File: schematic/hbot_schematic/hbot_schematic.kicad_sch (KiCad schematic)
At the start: 23 parts, among them M1 Nema 17, M2 Nema 23, M3 Nema 17, M4 Nema 14, M5 Nema 14, M6 Nema 14, U1 Teensy4.1

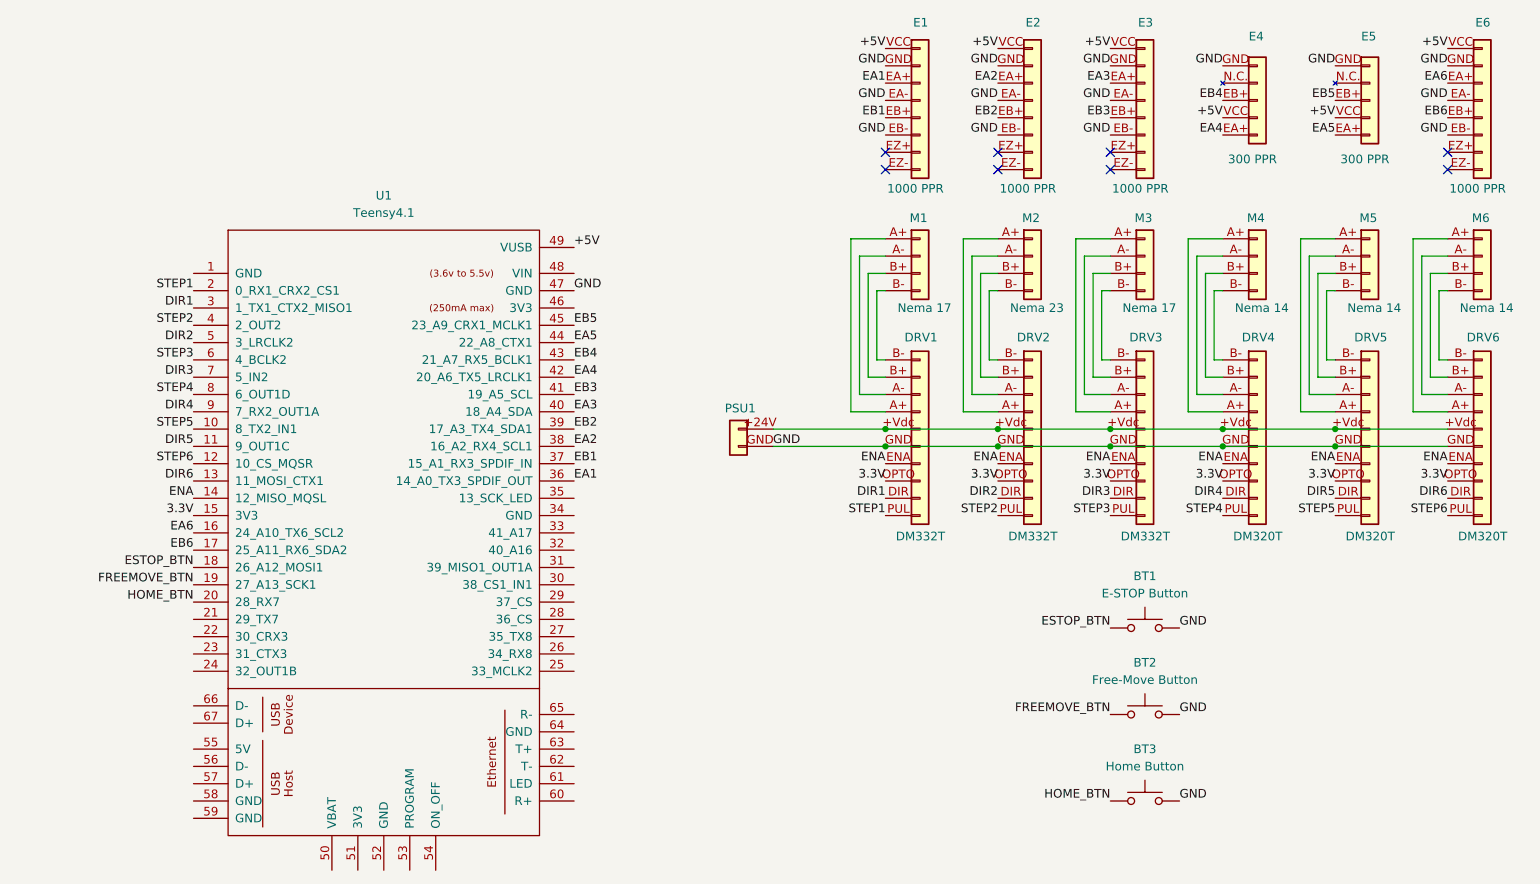
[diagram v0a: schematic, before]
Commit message: updated with hardware E-stop + software for redundancy. ujdpated readme, added schematic
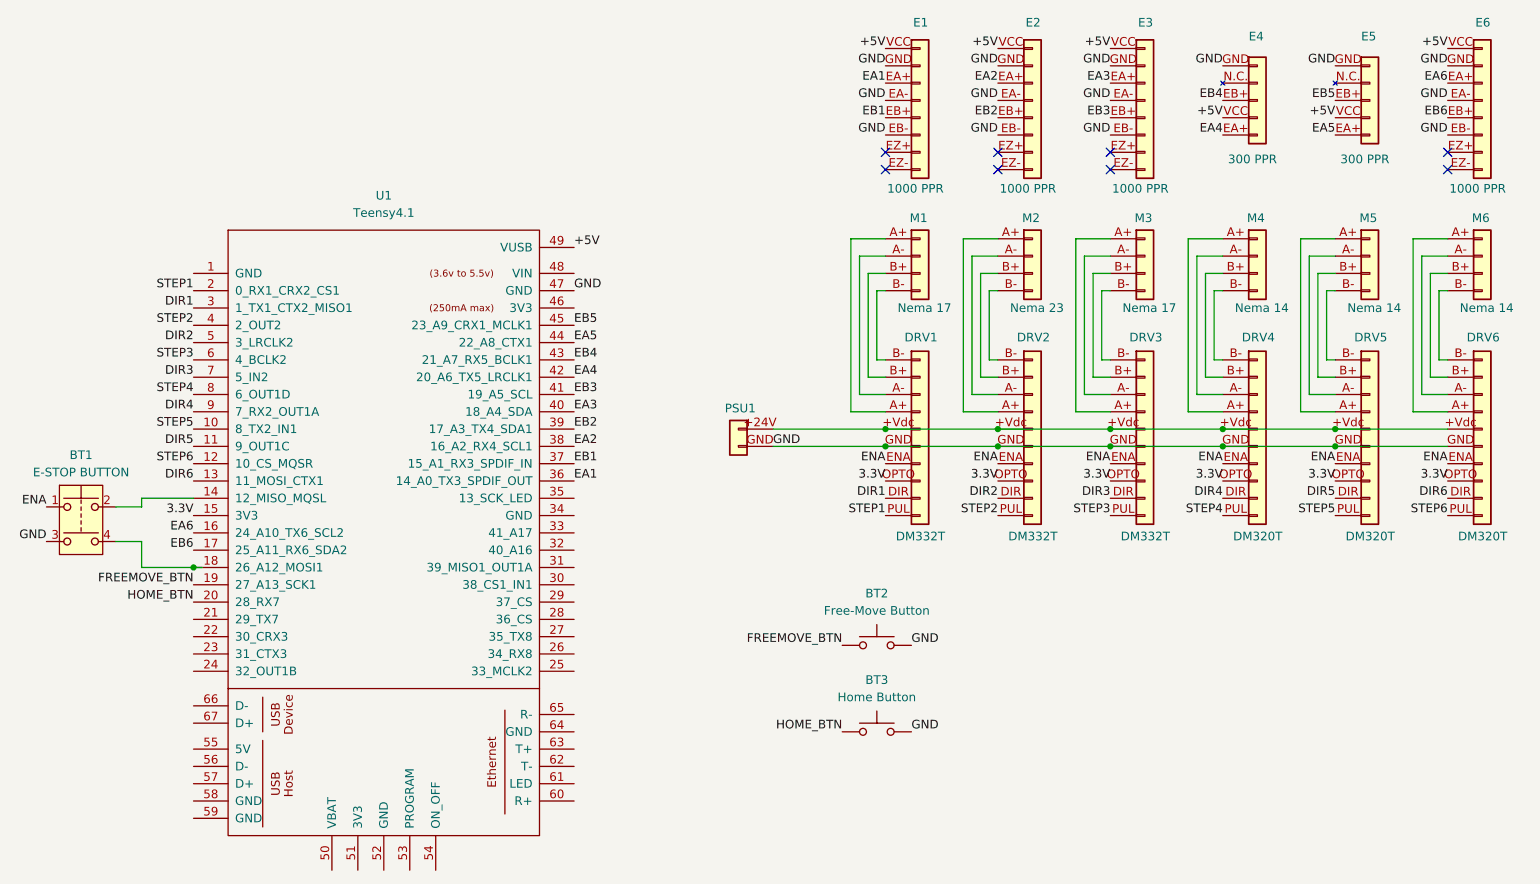
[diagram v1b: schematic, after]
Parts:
- removed BT1: E-STOP Button, symbol Switch:SW_Push
- added BT1: E-STOP BUTTON, symbol Switch:SW_Push_Dual
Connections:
- net ENA: now also BT1.1; no longer U1.14 (12_MISO_MQSL)
- net GND: now also BT1.3
- net ESTOP_BTN: no longer names the net of U1.18 (26_A12_MOSI1)
- net ESTOP_BTN: now also BT1.4
- new net: BT1.2, U1.14 (12_MISO_MQSL)
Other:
- moved on the sheet: BT2, BT3
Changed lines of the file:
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@@
 	)
 	(junction
+		(at 62.23 111.76)
+		(diameter 0)
+		(color 0 0 0 0)
+	)
+	(junction
 		(at 196.85 93.98)
 		(diameter 0)
@@
 	(wire
 		(pts
+			(xy 62.23 101.6) (xy 54.61 101.6)
+		)
+		(stroke
+			(width 0)
+			(type default)
+		)
+	)
+	(wire
+		(pts
 			(xy 193.04 66.04) (xy 196.85 66.04)
 		)
@@
 	(wire
 		(pts
+			(xy 54.61 107.95) (xy 54.61 111.76)
+		)
+		(stroke
+			(width 0)
+			(type default)
+		)
+	)
+	(wire
+		(pts
 			(xy 180.34 91.44) (xy 196.85 91.44)
 		)
@@
 	(wire
 		(pts
+			(xy 50.8 107.95) (xy 54.61 107.95)
+		)
+		(stroke
+			(width 0)
+			(type default)
+		)
+	)
+	(wire
+		(pts
 			(xy 196.85 81.28) (xy 195.58 81.28)
 		)
@@
 	(wire
 		(pts
+			(xy 54.61 111.76) (xy 62.23 111.76)
+		)
+		(stroke
+			(width 0)
+			(type default)
+		)
+	)
+	(wire
+		(pts
 			(xy 195.58 81.28) (xy 195.58 71.12)
 		)
@@
 	(wire
 		(pts
+			(xy 54.61 101.6) (xy 54.61 102.87)
+		)
+		(stroke
+			(width 0)
+			(type default)
+		)
+	)
+	(wire
+		(pts
 			(xy 213.36 81.28) (xy 212.09 81.28)
 		)
@@
 	(wire
 		(pts
+			(xy 62.23 111.76) (xy 63.5 111.76)
+		)
+		(stroke
+			(width 0)
+			(type default)
+		)
+	)
+	(wire
+		(pts
 			(xy 180.34 86.36) (xy 176.53 86.36)
 		)
@@
 		)
 	)
+	(wire
+		(pts
+			(xy 54.61 102.87) (xy 50.8 102.87)
+		)
+		(stroke
+			(width 0)
+			(type default)
+		)
+	)
 	(label "STEP4"
 		(at 62.23 86.36 180)
@@
 		)
 	)
-	(label "ENA"
-		(at 62.23 101.6 180)
-		(effects
-			(font
-				(size 1.27 1.27)
-			)
-			(justify right bottom)
-		)
-	)
 	(label "GND"
 		(at 246.38 43.18 180)
@@
 		)
 	)
-	(label "ESTOP_BTN"
-		(at 196.85 120.65 180)
-		(effects
-			(font
-				(size 1.27 1.27)
-			)
-			(justify right bottom)
-		)
-	)
 	(label "HOME_BTN"
-		(at 196.85 146.05 180)
+		(at 157.48 135.89 180)
 		(effects
 			(font
@@
 	)
 	(label "FREEMOVE_BTN"
-		(at 196.85 133.35 180)
+		(at 157.48 123.19 180)
 		(effects
 			(font
@@
 	)
 	(label "GND"
-		(at 207.01 120.65 0)
+		(at 167.64 123.19 0)
 		(effects
 			(font
@@
 	)
 	(label "GND"
-		(at 207.01 133.35 0)
+		(at 167.64 135.89 0)
 		(effects
 			(font
@@
 		)
 	)
-	(label "GND"
-		(at 207.01 146.05 0)
+	(label "ENA"
+		(at 40.64 102.87 180)
 		(effects
 			(font
 				(size 1.27 1.27)
 			)
-			(justify left bottom)
+			(justify right bottom)
 		)
 	)
@@
 		)
 	)
-	(label "FREEMOVE_BTN"
-		(at 62.23 114.3 180)
+	(label "GND"
+		(at 40.64 107.95 180)
 		(effects
 			(font
@@
 		)
 	)
-	(label "DIR1"
-		(at 62.23 73.66 180)
+	(label "FREEMOVE_BTN"
+		(at 62.23 114.3 180)
 		(effects
 			(font
@@
 		)
 	)
-	(label "ESTOP_BTN"
-		(at 62.23 111.76 180)
+	(label "DIR1"
+		(at 62.23 73.66 180)
 		(effects
 			(font
@@
 	)
 	(symbol
-		(lib_id "Switch:SW_Push")
-		(at 201.93 120.65 0)
-		(unit 1)
-		(exclude_from_sim no)
-		(in_bom yes)
-		(on_board yes)
-		(dnp no)
-		(fields_autoplaced yes)
-		(property "Reference" "BT1"
-			(at 201.93 113.03 0)
-			(effects
-				(font
-					(size 1.27 1.27)
-				)
-			)
-		)
-		(property "Value" "E-STOP Button"
-			(at 201.93 115.57 0)
-			(effects
-				(font
-					(size 1.27 1.27)
-				)
-			)
-		)
-		(property "Footprint" ""
-			(at 201.93 115.57 0)
-			(effects
-				(font
-					(size 1.27 1.27)
-				)
-				(hide yes)
-			)
-		)
-		(property "Datasheet" "~"
-			(at 201.93 115.57 0)
-			(effects
-				(font
-					(size 1.27 1.27)
-				)
-				(hide yes)
-			)
-		)
-		(property "Description" "Push button switch, generic, two pins"
-			(at 201.93 120.65 0)
-			(effects
-				(font
-					(size 1.27 1.27)
-				)
-				(hide yes)
-			)
-		)
-		(pin "2"
-		)
-		(pin "1"
-		)
-		(instances
-			(project ""
-				(path "/bc1e725a-6633-4704-8d72-fa9ba85f98b3"
-					(reference "BT1")
-					(unit 1)
-				)
-			)
-		)
-	)
-	(symbol
 		(lib_id "Connector_Generic:Conn_01x04")
 		(at 168.91 66.04 0)
@@
 	(symbol
 		(lib_id "Switch:SW_Push")
-		(at 201.93 133.35 0)
+		(at 162.56 123.19 0)
 		(unit 1)
 		(exclude_from_sim no)
@@
 		(fields_autoplaced yes)
 		(property "Reference" "BT2"
-			(at 201.93 125.73 0)
+			(at 162.56 115.57 0)
 			(effects
 				(font
@@
 		)
 		(property "Value" "Free-Move Button"
-			(at 201.93 128.27 0)
+			(at 162.56 118.11 0)
 			(effects
 				(font
@@
 		)
 		(property "Footprint" ""
-			(at 201.93 128.27 0)
+			(at 162.56 118.11 0)
 			(effects
 				(font
@@
 		)
 		(property "Datasheet" "~"
-			(at 201.93 128.27 0)
+			(at 162.56 118.11 0)
 			(effects
 				(font
@@
 		)
 		(property "Description" "Push button switch, generic, two pins"
-			(at 201.93 133.35 0)
+			(at 162.56 123.19 0)
 			(effects
 				(font
@@
 	(symbol
 		(lib_id "Switch:SW_Push")
-		(at 201.93 146.05 0)
+		(at 162.56 135.89 0)
 		(unit 1)
 		(exclude_from_sim no)
@@
 		(fields_autoplaced yes)
 		(property "Reference" "BT3"
-			(at 201.93 138.43 0)
+			(at 162.56 128.27 0)
 			(effects
 				(font
@@
 		)
 		(property "Value" "Home Button"
-			(at 201.93 140.97 0)
+			(at 162.56 130.81 0)
 			(effects
 				(font
@@
 		)
 		(property "Footprint" ""
-			(at 201.93 140.97 0)
+			(at 162.56 130.81 0)
 			(effects
 				(font
@@
 		)
 		(property "Datasheet" "~"
-			(at 201.93 140.97 0)
+			(at 162.56 130.81 0)
 			(effects
 				(font
@@
 		)
 		(property "Description" "Push button switch, generic, two pins"
-			(at 201.93 146.05 0)
+			(at 162.56 135.89 0)
 			(effects
 				(font
@@
 					(unit 1)
 				)
+			)
+		)
+	)
+	(symbol
+		(lib_id "Switch:SW_Push_Dual")
+		(at 45.72 105.41 0)
+		(unit 1)
+		(exclude_from_sim no)
+		(in_bom yes)
+		(on_board yes)
+		(dnp no)
+		(fields_autoplaced yes)
+		(property "Reference" "BT1"
+			(at 45.72 95.25 0)
+			(effects
+				(font
+					(size 1.27 1.27)
+				)
+			)
+		)
+		(property "Value" "E-STOP BUTTON"
+			(at 45.72 97.79 0)
+			(effects
+				(font
+					(size 1.27 1.27)
+				)
+			)
+		)
+		(property "Footprint" ""
+			(at 45.72 97.79 0)
+			(effects
+				(font
+					(size 1.27 1.27)
+				)
+				(hide yes)
+			)
+		)
+		(property "Datasheet" "~"
+			(at 45.72 105.41 0)
+			(effects
+				(font
+					(size 1.27 1.27)
+				)
+				(hide yes)
+			)
+		)
+		(property "Description" "Push button switch, generic, symbol, four pins"
+			(at 45.72 105.41 0)
+			(effects
+				(font
+					(size 1.27 1.27)
+				)
+				(hide yes)
+			)
+		)
+		(pin "4"
+		)
+		(pin "1"
+		)
+		(pin "3"
+		)
+		(pin "2"
+		)
+		(instances
+			(project ""
+				(path "/bc1e725a-6633-4704-8d72-fa9ba85f98b3"
+					(reference "BT1")
+					(unit 1)
+				)
